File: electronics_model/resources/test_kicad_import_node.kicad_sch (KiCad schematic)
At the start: 3 parts

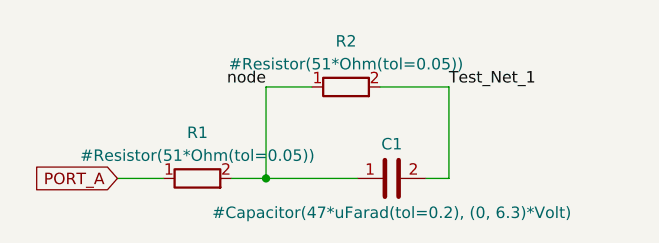
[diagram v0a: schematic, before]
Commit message: Refactor examples / libraries to use import KiCad schematics (#184)
Refactors a lot of analog blocks (most opamp topologies, analog
switches) to be KiCad importable blocks (by defining a symbol pin
mapping) and/or KiCad imported schematics. Adds custom symbols for many
of these parts, some KiCad's base symbol library for the most part lacks
abstract / generic and high-level parts.

Netlists of example designs should not have changed.

KiCad import behavior change:
- global labels must connect to either a node or external block port and
are not treated as link names
- net labels are used as link names and must not collide with any
existing object member
- add unit tests for the above
- schematic now works on a fixed grid so points can be rounded to the
nearest point that lines up - it turns out points on schematic files can
be off by like 0.05 or something which broke the previous netlister
- support power nets (eg, GND, Vcc symbols)
- power nets and all labels are treated as connected in the schematic
importer (instead of punted up to the block to be handled as connected
in separate connect statements)
- support inline modified symbols (lib_name vs lib_id)
- support symbol mirror, fix rotation calculation (and unit test all of
this)
- import blocks in schematic in xy order (or optionally file order -
this isn't used)
- add a `file_path` utility function to KiCadSchematicBlock which
returns a relative path from the calling file
- moves some tests (mainly rotation, mirror, symbol connectivity) to be
schematic parser tests only, because it's a bit extra (and probably
doesn't tell us much more) to go all the way to Block proto

Infrastructural changes:
- refactors some existing symbol mappings to use pin names instead of
numbers
- refactors some existing symbol mappings to use Mapping return type
which is type covariant
- for connection type errors (link inference errors), prints the names
of the ports involved
- some better error 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
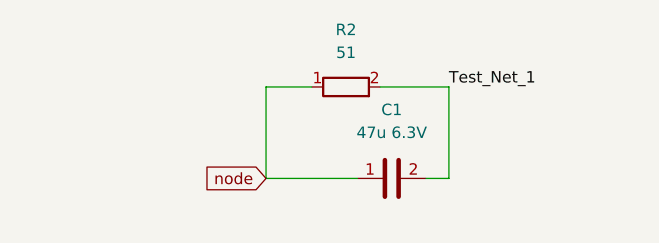
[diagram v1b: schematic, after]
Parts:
- removed R2: #Resistor(51*Ohm(tol=0.05)), symbol Device:R
- C1: value #Capacitor(47*uFarad(tol=0.2), (0, 6.3)*Volt) -> 47u 6.3V
- R2: renamed from R1; value #Resistor(51*Ohm(tol=0.05)) -> 51
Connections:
- net PORT_A is gone; now on net node: R2.1
- net Test_Net_1: now also R2.2
- net node: no longer R2.2
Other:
- moved on the sheet: R2
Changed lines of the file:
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@@
     (rev "v01")
-  )
-  (junction (at 91.44 96.52) (diameter 0) (color 0 0 0 0)
   )
   (wire (pts (xy 91.44 86.36) (xy 91.44 96.52))
@@
     (stroke (width 0) (type default) (color 0 0 0 0))
   )
-  (wire (pts (xy 74.93 96.52) (xy 80.01 96.52))
-    (stroke (width 0) (type default) (color 0 0 0 0))
-  )
   (wire (pts (xy 91.44 86.36) (xy 96.52 86.36))
-    (stroke (width 0) (type default) (color 0 0 0 0))
-  )
-  (wire (pts (xy 87.63 96.52) (xy 91.44 96.52))
     (stroke (width 0) (type default) (color 0 0 0 0))
   )
@@
     (stroke (width 0) (type default) (color 0 0 0 0))
   )
-  (label "node" (at 91.44 86.36 180)
-    (effects (font (size 1.27 1.27)) (justify right bottom))
-  )
   (label "Test_Net_1" (at 111.76 86.36 0)
     (effects (font (size 1.27 1.27)) (justify left bottom))
   )
-  (global_label "PORT_A" (shape input) (at 74.93 96.52 180) (fields_autoplaced)
+  (global_label "node" (shape input) (at 91.44 96.52 180) (fields_autoplaced)
     (effects (font (size 1.27 1.27)) (justify right))
-    (property "Intersheet References" "${INTERSHEET_REFS}" (id 0) (at 65.6226 96.4406 0)
+    (property "Intersheet References" "${INTERSHEET_REFS}" (id 0) (at 84.4912 96.4406 0)
       (effects (font (size 1.27 1.27)) (justify right) hide)
     )
   )
   (symbol (lib_id "Device:R") (at 100.33 86.36 90) (unit 1)
-    (in_bom yes) (on_board yes)
-    (property "Reference" "R2" (id 0) (at 100.33 81.28 90))
-    (property "Value" "#Resistor(51*Ohm(tol=0.05))" (id 1) (at 100.33 83.82 90))
+    (in_bom yes) (on_board yes) (fields_autoplaced)
+    (property "Reference" "R2" (id 0) (at 100.33 80.01 90))
+    (property "Value" "51" (id 1) (at 100.33 82.55 90))
     (property "Footprint" "" (id 2) (at 100.33 88.138 90)
       (effects (font (size 1.27 1.27)) hide)
@@
     (pin "2")
   )
-  (symbol (lib_id "Device:R") (at 83.82 96.52 90) (unit 1)
-    (in_bom yes) (on_board yes)
-    (property "Reference" "R1" (id 0) (at 83.82 91.44 90))
-    (property "Value" "#Resistor(51*Ohm(tol=0.05))" (id 1) (at 83.82 93.98 90))
-    (property "Footprint" "" (id 2) (at 83.82 98.298 90)
-      (effects (font (size 1.27 1.27)) hide)
-    )
-    (property "Datasheet" "~" (id 3) (at 83.82 96.52 0)
-      (effects (font (size 1.27 1.27)) hide)
-    )
-    (pin "1")
-    (pin "2")
-  )
   (symbol (lib_id "Device:C") (at 105.41 96.52 90) (unit 1)
-    (in_bom yes) (on_board yes)
-    (property "Reference" "C1" (id 0) (at 105.41 92.71 90))
-    (property "Value" "#Capacitor(47*uFarad(tol=0.2), (0, 6.3)*Volt)" (id 1) (at 105.41 100.33 90))
+    (in_bom yes) (on_board yes) (fields_autoplaced)
+    (property "Reference" "C1" (id 0) (at 105.41 88.9 90))
+    (property "Value" "47u 6.3V" (id 1) (at 105.41 91.44 90))
     (property "Footprint" "" (id 2) (at 109.22 95.5548 0)
       (effects (font (size 1.27 1.27)) hide)
@@
   (symbol_instances
     (path "/e8ed392d-e797-4a51-a62e-0d0cb2854712"
-      (reference "C1") (unit 1) (value "#Capacitor(47*uFarad(tol=0.2), (0, 6.3)*Volt)") (footprint "")
+      (reference "C1") (unit 1) (value "47u 6.3V") (footprint "")
     )
     (path "/691e9d02-a5cc-48a1-b9c1-b97da20de9cd"
-      (reference "R1") (unit 1) (value "#Resistor(51*Ohm(tol=0.05))") (footprint "")
-    )
-    (path "/1baff40e-08de-469f-a254-3c085c13e6e4"
-      (reference "R2") (unit 1) (value "#Resistor(51*Ohm(tol=0.05))") (footprint "")
+      (reference "R2") (unit 1) (value "51") (footprint "")
     )
   )

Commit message: unify naming
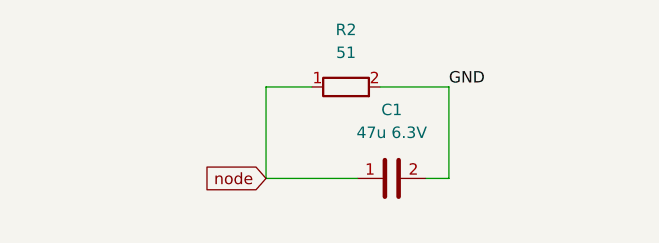
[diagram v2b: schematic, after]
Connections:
- net Test_Net_1 renamed GND
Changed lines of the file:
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@@
     (stroke (width 0) (type default) (color 0 0 0 0))
   )
-  (label "Test_Net_1" (at 111.76 86.36 0)
+  (label "GND" (at 111.76 86.36 0)
     (effects (font (size 1.27 1.27)) (justify left bottom))
   )
